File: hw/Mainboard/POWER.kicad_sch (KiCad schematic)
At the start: 63 parts, among them J1 9V POWER, J2 9V POWER, J3 PET POWER, J4 5V PWR, U3 LM317AG-TN3-R, U4 XL1509-5.0E1, U5 LM317AG-TN3-R, U6 AMS1117-3.3

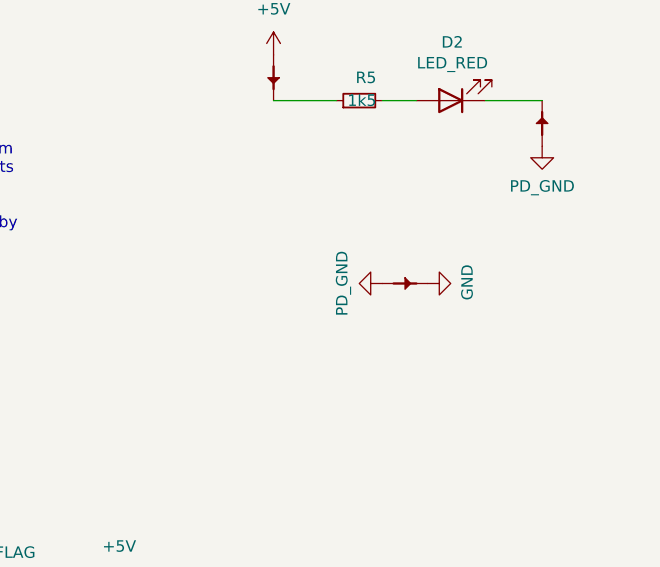
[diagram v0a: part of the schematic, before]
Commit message: hw: copper fills (wip, progress on buck converter)
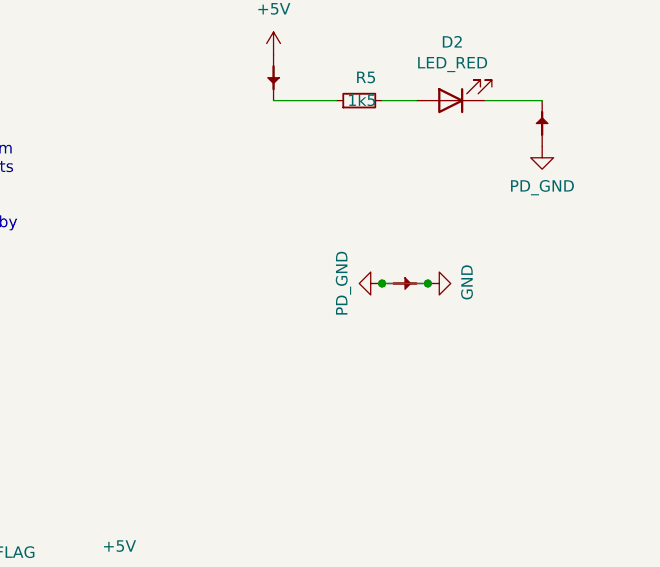
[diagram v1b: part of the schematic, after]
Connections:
- net PD_GND is gone; now on net GND: C10.2, C14.2, C15.2, C16.2, C17.2, C23.2, C24.2, C5.2, C6.2, C8.2, C86.2, C87.2, C89.2, C90.2, C91.2, D1.2 (A), D5.2 (A), J1.2, J1.3, J2.1 (Pin_1), J3.3 (GND), J3.6 (GND), J4.1 (Pin_1), J4.3 (Pin_3), J4.5 (Pin_5), PT10.1, PT11.1, PT4.1, R13.2, U4.4 (~{EN}), U4.5 (GND), U4.6 (GND), U4.7 (GND), U4.8 (GND), U6.1 (GND)
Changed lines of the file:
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@@
   (junction (at 106.68 92.71) (diameter 0) (color 0 0 0 0)
   )
+  (junction (at 240.03 58.42) (diameter 0) (color 0 0 0 0)
+  )
   (junction (at 116.84 36.83) (diameter 0) (color 0 0 0 0)
   )
@@
   )
   (junction (at 119.38 186.69) (diameter 0) (color 0 0 0 0)
+  )
+  (junction (at 245.11 58.42) (diameter 0) (color 0 0 0 0)
   )
   (junction (at 123.19 106.68) (diameter 0) (color 0 0 0 0)
@@
     (stroke (width 0) (type default) (color 0 0 0 0))
   )
+  (wire (pts (xy 240.03 58.42) (xy 245.11 58.42))
+    (stroke (width 0) (type default) (color 0 0 0 0))
+  )

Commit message: hw: fill, routing, and silk touchups (wip)
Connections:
- net GND: now also D2.1 (K), PT4.2
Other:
- note removed: "Power headersnear IEEE and User ports for peripherals like PETdisk MAX and SNES adapter."
- moved on the sheet: C10, C14, C15, C16, C17, C18, C19, C20, C21, C22, C23, C24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

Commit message: hw: 5V decoupling caps, routing touch ups (wip)
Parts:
- added C97: 10u, Capacitor_SMD:C_0603_1608Metric, symbol Device:C_Small
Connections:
- net +5V: now also C97.1
- net GND: now also C97.2
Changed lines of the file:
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@@
   (junction (at 143.51 46.99) (diameter 0) (color 0 0 0 0)
   )
+  (junction (at 246.38 143.51) (diameter 0) (color 0 0 0 0)
+  )
   (junction (at 223.52 92.71) (diameter 0) (color 0 0 0 0)
   )
@@
   (junction (at 143.51 44.45) (diameter 0) (color 0 0 0 0)
   )
+  (junction (at 254 151.13) (diameter 0) (color 0 0 0 0)
+  )
   (junction (at 185.42 92.71) (diameter 0) (color 0 0 0 0)
   )
@@
   (junction (at 119.38 92.71) (diameter 0) (color 0 0 0 0)
   )
+  (junction (at 261.62 143.51) (diameter 0) (color 0 0 0 0)
+  )
   (junction (at 247.65 88.9) (diameter 0) (color 0 0 0 0)
   )
@@
   )
   (junction (at 128.27 106.68) (diameter 0) (color 0 0 0 0)
-  )
-  (junction (at 246.38 143.51) (diameter 0) (color 0 0 0 0)
   )
   (junction (at 147.32 177.8) (diameter 0) (color 0 0 0 0)
@@
     (stroke (width 0) (type default) (color 0 0 0 0))
   )
+  (wire (pts (xy 261.62 143.51) (xy 261.62 144.78))
+    (stroke (width 0) (type default) (color 0 0 0 0))
+  )
   (wire (pts (xy 246.38 138.43) (xy 246.38 140.97))
     (stroke (width 0) (type default) (color 0 0 0 0))
@@
     (stroke (width 0) (type default) (color 0 0 0 0))
   )
+  (wire (pts (xy 261.62 149.86) (xy 261.62 151.13))
+    (stroke (width 0) (type default) (color 0 0 0 0))
+  )
   (wire (pts (xy 133.35 129.54) (xy 139.7 129.54))
     (stroke (width 0) (type default) (color 0 0 0 0))
@@
     (stroke (width 0) (type default) (color 0 0 0 0))
   )
+  (wire (pts (xy 254 151.13) (xy 246.38 151.13))
+    (stroke (width 0) (type default) (color 0 0 0 0))
+  )
   (wire (pts (xy 132.08 186.69) (xy 147.32 186.69))
     (stroke (width 0) (type default) (color 0 0 0 0))
@@
     (stroke (width 0) (type default) (color 0 0 0 0))
   )
+  (wire (pts (xy 246.38 151.13) (xy 246.38 143.51))
+    (stroke (width 0) (type default) (color 0 0 0 0))
+  )
   (wire (pts (xy 170.18 140.97) (xy 180.34 140.97))
     (stroke (width 0) (type default) (color 0 0 0 0))
@@
     (stroke (width 0) (type default) (color 0 0 0 0))
   )
+  (wire (pts (xy 261.62 151.13) (xy 254 151.13))
+    (stroke (width 0) (type default) (color 0 0 0 0))
+  )
   (wire (pts (xy 143.51 154.94) (xy 143.51 148.59))
     (stroke (width 0) (type default) (color 0 0 0 0))
@@
     (stroke (width 0) (type default) (color 0 0 0 0))
   )
-  (wire (pts (xy 246.38 143.51) (xy 246.38 144.78))
-    (stroke (width 0) (type default) (color 0 0 0 0))
-  )
   (wire (pts (xy 49.53 74.93) (xy 49.53 81.28))
     (stroke (width 0) (type default) (color 0 0 0 0))
@@
   )
   (wire (pts (xy 76.2 74.93) (xy 80.01 74.93))
+    (stroke (width 0) (type default) (color 0 0 0 0))
+  )
+  (wire (pts (xy 254 151.13) (xy 254 152.4))
     (stroke (width 0) (type default) (color 0 0 0 0))
   )
@@
     (pin "1")
   )
+  (symbol (lib_id "Device:C_Small") (at 261.62 147.32 0) (mirror y) (unit 1)
+    (in_bom yes) (on_board yes)
+    (property "Reference" "C97" (id 0) (at 259.2832 146.1516 0)
+      (effects (font (size 1.27 1.27)) (justify left))
+    )
+    (property "Value" "10u" (id 1) (at 259.2832 148.463 0)
+      (effects (font (size 1.27 1.27)) (justify left))
+    )
+    (property "Footprint" "Capacitor_SMD:C_0603_1608Metric" (id 2) (at 261.62 147.32 0)
+      (effects (font (size 1.27 1.27)) hide)
+    )
+    (property "Datasheet" "https://datasheet.lcsc.com/lcsc/2304140030_Samsung-Electro-Mechanics-CL10A106MA8NRNC_C96446.pdf" (id 3) (at 261.62 147.32 0)
+      (effects (font (size 1.27 1.27)) hide)
+    )
+    (property "LCSC" "C96446" (id 4) (at 261.62 147.32 0)
+      (effects (font (size 1.27 1.27)) hide)
+    )
+    (pin "1")
+    (pin "2")
+  )
   (symbol (lib_id "Device:C_Small") (at 165.1 99.06 0) (unit 1)
     (in_bom yes) (on_board yes)
@@
     (pin "1")
   )
-  (symbol (lib_id "PET:PD_GND") (at 246.38 144.78 0) (unit 1)
-    (in_bom yes) (on_board yes)
-    (property "Reference" "#PWR021" (id 0) (at 246.38 151.13 0)
-      (effects (font (size 1.27 1.27)) hide)
-    )
-    (property "Value" "PD_GND" (id 1) (at 246.38 149.225 0))
-    (property "Footprint" "" (id 2) (at 246.38 144.78 0)
-      (effects (font (size 1.27 1.27)) hide)
-    )
-    (property "Datasheet" "" (id 3) (at 246.38 144.78 0)
-      (effects (font (size 1.27 1.27)) hide)
-    )
+  (symbol (lib_id "PET:PD_GND") (at 254 152.4 0) (unit 1)
+    (in_bom yes) (on_board yes)
+    (property "Reference" "#PWR021" (id 0) (at 254 158.75 0)
+      (effects (font (size 1.27 1.27)) hide)
+    )
+    (property "Value" "PD_GND" (id 1) (at 254 156.845 0))
+    (property "Footprint" "" (id 2) (at 254 152.4 0)
+      (effects (font (size 1.27 1.27)) hide)
+    )
+    (property "Datasheet" "" (id 3) (at 254 152.4 0)
+      (effects (font (size 1.27 1.27)) hide)
+    )

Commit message: hw: touch ups / avoid a few uniques (wip)
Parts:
- C8: footprint Capacitor_SMD:C_0603_1608Metric -> Capacitor_SMD:C_0402_1005Metric; LCSC C15849 -> C52923
- D1, D4, D5, D6: value SS34 -> SS54; LCSC C8678 -> C22452
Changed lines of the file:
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@@
     (in_bom yes) (on_board yes)
     (property "Reference" "D4" (id 0) (at 70.231 62.484 90))
-    (property "Value" "SS34" (id 1) (at 71.501 64.643 90))
+    (property "Value" "SS54" (id 1) (at 71.501 64.643 90))
     (property "Footprint" "Diode_SMD:D_SMA" (id 2) (at 67.31 63.5 90)
       (effects (font (size 1.27 1.27)) hide)
     )
-    (property "Datasheet" "https://datasheet.lcsc.com/lcsc/2303141100_MDD-Microdiode-Electronics--SS34_C8678.pdf" (id 3) (at 67.31 63.5 90)
-      (effects (font (size 1.27 1.27)) hide)
-    )
-    (property "LCSC" "C8678" (id 4) (at 67.31 63.5 0)
+    (property "Datasheet" "" (id 3) (at 67.31 63.5 90)
+      (effects (font (size 1.27 1.27)) hide)
+    )
+    (property "LCSC" "C22452" (id 4) (at 67.31 63.5 0)
       (effects (font (size 1.27 1.27)) hide)
     )
@@
     (in_bom yes) (on_board yes)
     (property "Reference" "D6" (id 0) (at 70.231 69.977 90))
-    (property "Value" "SS34" (id 1) (at 71.374 72.263 90))
+    (property "Value" "SS54" (id 1) (at 71.374 72.263 90))
     (property "Footprint" "Diode_SMD:D_SMA" (id 2) (at 67.31 71.12 90)
       (effects (font (size 1.27 1.27)) hide)
     )
-    (property "Datasheet" "https://datasheet.lcsc.com/lcsc/2303141100_MDD-Microdiode-Electronics--SS34_C8678.pdf" (id 3) (at 67.31 71.12 90)
-      (effects (font (size 1.27 1.27)) hide)
-    )
-    (property "LCSC" "C8678" (id 4) (at 67.31 71.12 0)
+    (property "Datasheet" "" (id 3) (at 67.31 71.12 90)
+      (effects (font (size 1.27 1.27)) hide)
+    )
+    (property "LCSC" "C22452" (id 4) (at 67.31 71.12 0)
       (effects (font (size 1.27 1.27)) hide)
     )
@@
     (in_bom yes) (on_board yes)
     (property "Reference" "D5" (id 0) (at 54.737 62.738 0))
-    (property "Value" "SS34" (id 1) (at 55.88 64.77 0))
+    (property "Value" "SS54" (id 1) (at 55.88 64.77 0))
     (property "Footprint" "Diode_SMD:D_SMA" (id 2) (at 55.88 67.31 90)
       (effects (font (size 1.27 1.27)) hide)
     )
-    (property "Datasheet" "https://datasheet.lcsc.com/lcsc/2303141100_MDD-Microdiode-Electronics--SS34_C8678.pdf" (id 3) (at 55.88 67.31 90)
-      (effects (font (size 1.27 1.27)) hide)
-    )
-    (property "LCSC" "C8678" (id 4) (at 55.88 67.31 0)
+    (property "Datasheet" "" (id 3) (at 55.88 67.31 90)
+      (effects (font (size 1.27 1.27)) hide)
+    )
+    (property "LCSC" "C22452" (id 4) (at 55.88 67.31 0)
       (effects (font (size 1.27 1.27)) hide)
     )
@@
       (effects (font (size 1.27 1.27)) (justify left))
     )
-    (property "Footprint" "Capacitor_SMD:C_0603_1608Metric" (id 2) (at 119.38 99.06 0)
-      (effects (font (size 1.27 1.27)) hide)
-    )
-    (property "Datasheet" "https://datasheet.lcsc.com/lcsc/1810261812_Samsung-Electro-Mechanics-CL10A105KB8NNNC_C15849.pdf" (id 3) (at 119.38 99.06 0)
-      (effects (font (size 1.27 1.27)) hide)
-    )
-    (property "LCSC" "C15849" (id 4) (at 119.38 99.06 0)
+    (property "Footprint" "Capacitor_SMD:C_0402_1005Metric" (id 2) (at 119.38 99.06 0)
+      (effects (font (size 1.27 1.27)) hide)
+    )
+    (property "Datasheet" "https://datasheet.lcsc.com/lcsc/2304140030_Samsung-Electro-Mechanics-CL05A105KA5NQNC_C52923.pdf" (id 3) (at 119.38 99.06 0)
+      (effects (font (size 1.27 1.27)) hide)
+    )
+    (property "LCSC" "C52923" (id 4) (at 119.38 99.06 0)
       (effects (font (size 1.27 1.27)) hide)
     )
@@
     (in_bom yes) (on_board yes)
     (property "Reference" "D1" (id 0) (at 152.019 100.076 90))
-    (property "Value" "SS34" (id 1) (at 150.749 97.917 90))
+    (property "Value" "SS54" (id 1) (at 150.749 97.917 90))
     (property "Footprint" "Diode_SMD:D_SMA" (id 2) (at 154.94 99.06 90)
       (effects (font (size 1.27 1.27)) hide)
     )
-    (property "Datasheet" "https://datasheet.lcsc.com/lcsc/2204121115_MDD-Microdiode-Electronics--SS34_C8678.pdf" (id 3) (at 154.94 99.06 90)
-      (effects (font (size 1.27 1.27)) hide)
-    )
-    (property "LCSC" "C8678" (id 4) (at 154.94 99.06 0)
-      (effects (font (size 1.27 1.27)) hide)
-    )
+    (property "Datasheet" "" (id 3) (at 154.94 99.06 90)
+      (effects (font (size 1.27 1.27)) hide)
+    )
+    (property "LCSC" "C22452" (id 4) (at 154.94 99.06 0)
+      (effects (font (size 1.27 1.27)) hide)
+    )

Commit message: hw: touch ups (wip)
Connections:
- net +5V: now also C22.1, PT12.2
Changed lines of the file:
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@@
   (junction (at 63.5 36.83) (diameter 0) (color 0 0 0 0)
+  )
+  (junction (at 124.46 147.32) (diameter 0) (color 0 0 0 0)
+  )
+  (junction (at 124.46 142.24) (diameter 0) (color 0 0 0 0)
   )
   (junction (at 49.53 67.31) (diameter 0) (color 0 0 0 0)
@@
     (stroke (width 0) (type default) (color 0 0 0 0))
   )
+  (wire (pts (xy 124.46 142.24) (xy 124.46 147.32))
+    (stroke (width 0) (type default) (color 0 0 0 0))
+  )

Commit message: hw: touchups (wip)
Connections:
- net +5V: now also PT2.2, R5.1
- net 9V_UNFILT: now also C11.2, C12.1, C13.2, PT6.2, PT7.2, PT9.2
- net GND: now also C13.1, PT10.2
- net VAC1: now also C11.1, PT5.2
- net VAC2: now also C12.2, PT8.2
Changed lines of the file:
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@@
   (junction (at 82.55 36.83) (diameter 0) (color 0 0 0 0)
   )
+  (junction (at 74.93 68.58) (diameter 0) (color 0 0 0 0)
+  )
   (junction (at 114.3 177.8) (diameter 0) (color 0 0 0 0)
   )
+  (junction (at 242.57 33.02) (diameter 0) (color 0 0 0 0)
+  )
   (junction (at 195.58 154.94) (diameter 0) (color 0 0 0 0)
   )
@@
   (junction (at 82.55 45.72) (diameter 0) (color 0 0 0 0)
   )
+  (junction (at 60.96 78.74) (diameter 0) (color 0 0 0 0)
+  )
+  (junction (at 76.2 59.69) (diameter 0) (color 0 0 0 0)
+  )
   (junction (at 261.62 138.43) (diameter 0) (color 0 0 0 0)
   )
@@
   (junction (at 195.58 106.68) (diameter 0) (color 0 0 0 0)
   )
+  (junction (at 80.01 68.58) (diameter 0) (color 0 0 0 0)
+  )
   (junction (at 209.55 92.71) (diameter 0) (color 0 0 0 0)
   )
@@
   (junction (at 223.52 92.71) (diameter 0) (color 0 0 0 0)
   )
+  (junction (at 71.12 59.69) (diameter 0) (color 0 0 0 0)
+  )
   (junction (at 110.49 106.68) (diameter 0) (color 0 0 0 0)
   )
@@
   (junction (at 73.66 45.72) (diameter 0) (color 0 0 0 0)
   )
+  (junction (at 76.2 74.93) (diameter 0) (color 0 0 0 0)
+  )
   (junction (at 73.66 36.83) (diameter 0) (color 0 0 0 0)
   )
@@
   (junction (at 195.58 140.97) (diameter 0) (color 0 0 0 0)
   )
+  (junction (at 242.57 38.1) (diameter 0) (color 0 0 0 0)
+  )
   (junction (at 165.1 92.71) (diameter 0) (color 0 0 0 0)
   )
@@
   (junction (at 147.32 177.8) (diameter 0) (color 0 0 0 0)
   )
+  (junction (at 60.96 73.66) (diameter 0) (color 0 0 0 0)
+  )
   (junction (at 132.08 186.69) (diameter 0) (color 0 0 0 0)
   )
@@
   (junction (at 114.3 140.97) (diameter 0) (color 0 0 0 0)
   )
+  (junction (at 54.61 81.28) (diameter 0) (color 0 0 0 0)
+  )
   (junction (at 175.26 92.71) (diameter 0) (color 0 0 0 0)
   )
   (junction (at 260.35 43.18) (diameter 0) (color 0 0 0 0)
   )
+  (junction (at 74.93 66.04) (diameter 0) (color 0 0 0 0)
+  )
   (junction (at 143.51 54.61) (diameter 0) (color 0 0 0 0)
   )
+  (junction (at 80.01 66.04) (diameter 0) (color 0 0 0 0)
+  )
   (junction (at 158.75 140.97) (diameter 0) (color 0 0 0 0)
   )
@@
   )
   (junction (at 195.58 92.71) (diameter 0) (color 0 0 0 0)
+  )
+  (junction (at 71.12 74.93) (diameter 0) (color 0 0 0 0)
   )
   (no_connect (at 35.56 80.01))
@@
     (stroke (width 0) (type default) (color 0 0 0 0))
   )
+  (wire (pts (xy 74.93 66.04) (xy 80.01 66.04))
+    (stroke (width 0) (type default) (color 0 0 0 0))
+  )
   (wire (pts (xy 124.46 147.32) (xy 124.46 154.94))
     (stroke (width 0) (type default) (color 0 0 0 0))
@@
     (stroke (width 0) (type default) (color 0 0 0 0))
   )
+  (wire (pts (xy 74.93 68.58) (xy 80.01 68.58))
+    (stroke (width 0) (type default) (color 0 0 0 0))
+  )
   (wire (pts (xy 246.38 151.13) (xy 246.38 143.51))
     (stroke (width 0) (type default) (color 0 0 0 0))
@@
     (stroke (width 0) (type default) (color 0 0 0 0))
   )
+  (wire (pts (xy 60.96 73.66) (xy 60.96 78.74))
+    (stroke (width 0) (type default) (color 0 0 0 0))
+  )
   (wire (pts (xy 195.58 101.6) (xy 195.58 106.68))
     (stroke (width 0) (type default) (color 0 0 0 0))
@@
     (stroke (width 0) (type default) (color 0 0 0 0))
   )
+  (wire (pts (xy 71.12 59.69) (xy 76.2 59.69))
+    (stroke (width 0) (type default) (color 0 0 0 0))
+  )
   (wire (pts (xy 223.52 92.71) (xy 223.52 96.52))
     (stroke (width 0) (type default) (color 0 0 0 0))
@@
     (stroke (width 0) (type default) (color 0 0 0 0))
   )
+  (wire (pts (xy 49.53 81.28) (xy 54.61 81.28))
+    (stroke (width 0) (type default) (color 0 0 0 0))
+  )
   (wire (pts (xy 185.42 92.71) (xy 195.58 92.71))
     (stroke (width 0) (type default) (color 0 0 0 0))
@@
     (stroke (width 0) (type default) (color 0 0 0 0))
   )
+  (wire (pts (xy 71.12 74.93) (xy 76.2 74.93))
+    (stroke (width 0) (type default) (color 0 0 0 0))
+  )
   (wire (pts (xy 135.89 80.01) (xy 135.89 85.09))
     (stroke (width 0) (type default) (color 0 0 0 0))
@@
     (stroke (width 0) (type default) (color 0 0 0 0))
   )
+  (wire (pts (xy 242.57 33.02) (xy 242.57 38.1))
+    (stroke (width 0) (type default) (color 0 0 0 0))
+  )

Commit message: hw: caps & logos (wip)
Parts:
- added SYM2: SYM_Arrow_Small, PET:EconoPET_QR, symbol Graphic:SYM_Arrow_Small
- added SYM3: SYM_Arrow_Small, PET:EconoPET_Model, symbol Graphic:SYM_Arrow_Small
- C97: value 10u -> 1u; footprint Capacitor_SMD:C_0603_1608Metric -> Capacitor_SMD:C_0402_1005Metric; LCSC C96446 -> C52923
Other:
- note added: "AMS1117 internal protection diodes are sufficient with output capacitors less than 1000uF."
- title: CBM PET Mainboard Replacement -> EconoPET 40/8096
- moved on the sheet: J4
